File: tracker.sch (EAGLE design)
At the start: 118 parts, among them J1 75869-131LF, J2 5-5530843-0FEMALE, J3 75869-131LF, Q1 DMG2302UK, Q2 CPC1002N, Q3 CPC1002N, Q4 MMBT3904, U1 AOZ6662DI, U2 ATMEGA328PB32-TQFP, U3 MCP1501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

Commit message: Various schematic updates
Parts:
- removed C7, C8: 1uF, radio-tracker:CAPACITOR0603
- removed R6: 10k, radio-tracker:RESISTOR0603
- removed U7: MIC5504, radio-tracker:MIC5504
- added J4: 640456-3, radio-tracker:640456-3
- added R44: 0R, radio-tracker:RESISTOR0603
- LS1: value WT-1205 -> AT-1224-TWT-5V-2-R; device radio-tracker:WT-1205 -> radio-tracker:AT-1224-TWT-5V-2-R
- R3: value 9.1k -> 4.7k
- R4: value 110k -> 68k
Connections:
- removed net +5V: A1.A, C14.P$2, C23.P$2, C6.P$2, C7.P$2, L1.P$2, LS1.P$2, R13.P$2, R4.P$2, R6.P$2, U7.VIN
- removed net N$11: R6.P$1, U7.EN
- new net N$43: C22.P$2
- net +3V3: now also A1.A, C14.P$2, C23.P$2, C6.P$2, L1.P$2, LS1.P$2, R13.P$2, R4.P$2; no longer C22.P$2, C8.P$2, U7.VOUT
- net GND: now also J4.GND; no longer C7.P$1, C8.P$1, U7.GND
- net MISO: now also R44.P$2
- net SCL: now also J4.SCL
- net SDA: now also J4.SDA
- net SLAVE_MISO: now also R44.P$1
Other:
- moved on the sheet: C12, C13, C2, C22, C23, C3, C4, C5, C6, L1, R14, R2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

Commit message: A few schematic updates
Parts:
- added C36, C8: 10uF, radio-tracker:CAPACITOR0805
- added C37: 0.01uF, radio-tracker:CAPACITOR0603
- added C38: 1uF, radio-tracker:CAPACITOR0603
- added C39, C7: 0.1uF, radio-tracker:CAPACITOR0603
- added C40: 22uF, radio-tracker:CAPACITOR0805
- added L2: 2.2uH, radio-tracker:INDUCTOR0805
- added R45, R46, R6: 10k, radio-tracker:RESISTOR0603
- added R47, R48, R49, R50: 0R, radio-tracker:RESISTOR0603
- added R52: 9.1k, radio-tracker:RESISTOR0603
- added R53: 110k, radio-tracker:RESISTOR0603
- added R54: 15k, radio-tracker:RESISTOR0603
- added U7: 47L16, radio-tracker:47L16
- added U8: AOZ6662DI, radio-tracker:AOZ6662DI
- R38: value (none) -> 10k
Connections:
- removed net N$2: S1.3, U1.EN
- new net +5V: C40.P$2, L2.P$2, R48.P$2, R49.P$2, R53.P$2
- new net N$11: R42.P$1, U6.E0
- new net N$44: C8.P$2, U7.VCAP
- new net N$45: R45.P$2, U7.A2
- new net N$46: R46.P$2, U7.A1
- new net N$50: R52.P$2, U8.COMP
- new net N$51: C2.P$2, R49.P$1, R50.P$1, U1.VIN
- new net N$52: C37.P$2, R52.P$1
- new net N$53: C38.P$2, U8.VCC
- new net N$54: C39.P$2, U8.BST
- new net N$55: C39.P$1, L2.P$1, U8.LX
- new net N$56: R53.P$1, R54.P$2, U8.FB
- new net PWR_EN: S1.3, U1.EN, U8.EN
- net +3V3: now also C22.P$2, C7.P$2, R42.P$2, R47.P$2, U7.VCC; no longer A1.A, C23.P$2
- net +7V4V: now also C36.P$2, R50.P$2, U8.VIN; no longer C2.P$2, U1.VIN
- net GND: now also C36.P$1, C37.P$1, C38.P$1, C40.P$1, C7.P$1, C8.P$1, R45.P$1, R46.P$1, R54.P$1, R6.P$1, U7.GND, U8.GND; no longer R42.P$1
- net N$38: now also R6.P$2, U7.HS; no longer R42.P$2, U6.E0
- net N$43: now also A1.A, C23.P$2, R47.P$1, R48.P$1; no longer C22.P$2
- net SCL: now also U7.SCL
- net SDA: now also U7.SDA
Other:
- moved on the sheet: C12, C13, C2, C22, C23, C3, C4, C5, C6, L1, R14, R2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

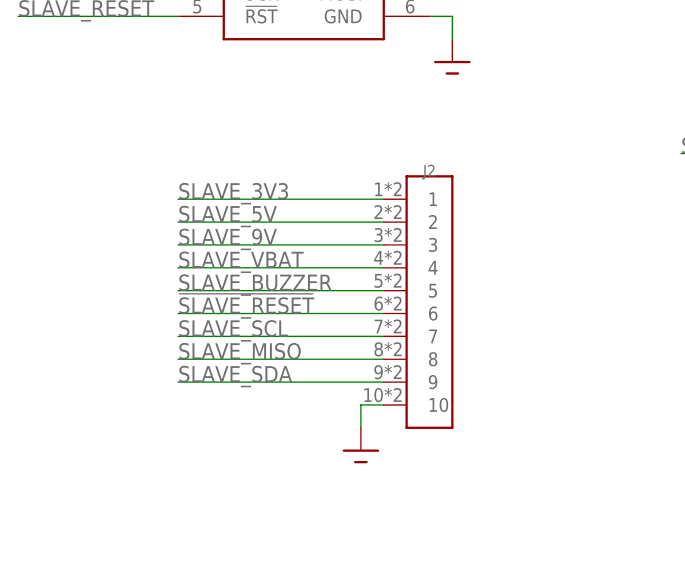
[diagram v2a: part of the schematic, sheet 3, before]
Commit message: Routed beacon
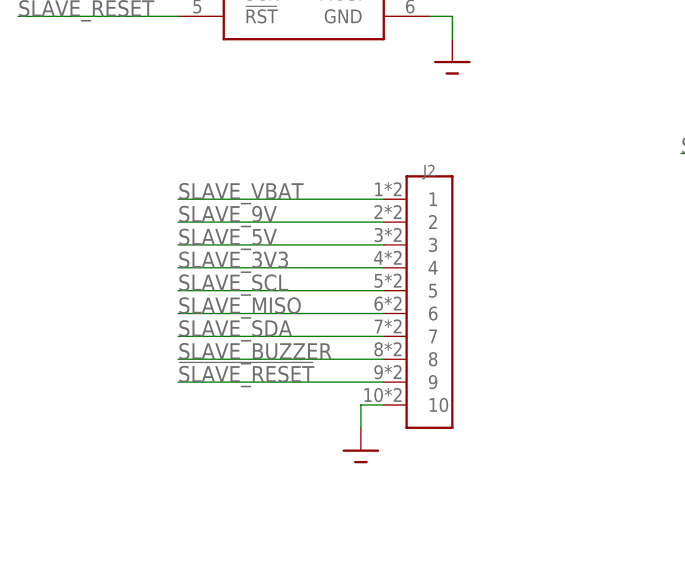
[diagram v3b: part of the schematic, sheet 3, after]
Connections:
- net !SLAVE_RESET: now also J2.9; no longer J2.6
- net SLAVE_3V3: now also J2.4; no longer J2.1
- net SLAVE_5V: now also J2.3; no longer J2.2
- net SLAVE_9V: now also J2.2; no longer J2.3
- net SLAVE_BUZZER: now also J2.8; no longer J2.5
- net SLAVE_MISO: now also J2.6; no longer J2.8
- net SLAVE_SCL: now also J2.5; no longer J2.7
- net SLAVE_SDA: now also J2.7; no longer J2.9
- net SLAVE_VBAT: now also J2.1; no longer J2.4
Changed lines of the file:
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@@
 <net name="SLAVE_SDA" class="0">
+<segment>
+<pinref part="J3" gate="G$1" pin="MOSI"/>
+<wire x1="38.1" y1="38.1" x2="20.32" y2="38.1" width="0.1524" layer="91"/>
+<label x="22.86" y="38.1" size="1.778" layer="95"/>
+</segment>
+<segment>
+<pinref part="J2" gate="G$1" pin="7"/>
+<wire x1="15.24" y1="0" x2="-7.62" y2="0" width="0.1524" layer="91"/>
+<label x="-7.62" y="0" size="1.778" layer="95"/>
+</segment>
+</net>
+<net name="SLAVE_MISO" class="0">
+<segment>
+<pinref part="J3" gate="G$1" pin="MISO"/>
+<wire x1="-7.62" y1="40.64" x2="-25.4" y2="40.64" width="0.1524" layer="91"/>
+<label x="-25.4" y="40.64" size="1.778" layer="95"/>
+</segment>
+<segment>
+<pinref part="R44" gate="G$1" pin="P$1"/>
+<wire x1="15.24" y1="-30.48" x2="-2.54" y2="-30.48" width="0.1524" layer="91"/>
+<label x="-2.54" y="-30.48" size="1.778" layer="95"/>
+</segment>
+<segment>
+<pinref part="J2" gate="G$1" pin="6"/>
+<wire x1="-7.62" y1="2.54" x2="15.24" y2="2.54" width="0.1524" layer="91"/>
+<label x="-7.62" y="2.54" size="1.778" layer="95"/>
+</segment>
+</net>
+<net name="SLAVE_SCL" class="0">
+<segment>
+<pinref part="J3" gate="G$1" pin="SCK"/>
+<wire x1="-25.4" y1="38.1" x2="-7.62" y2="38.1" width="0.1524" layer="91"/>
+<label x="-25.4" y="38.1" size="1.778" layer="95"/>
+</segment>
+<segment>
+<pinref part="J2" gate="G$1" pin="5"/>
+<wire x1="15.24" y1="5.08" x2="-7.62" y2="5.08" width="0.1524" layer="91"/>
+<label x="-7.62" y="5.08" size="1.778" layer="95"/>
+</segment>
+</net>
+<net name="!SLAVE_RESET" class="0">
+<segment>
+<pinref part="J3" gate="G$1" pin="!RST"/>
+<wire x1="-7.62" y1="35.56" x2="-25.4" y2="35.56" width="0.1524" layer="91"/>
+<label x="-25.4" y="35.56" size="1.778" layer="95"/>
+</segment>
 <segment>
 <pinref part="J2" gate="G$1" pin="9"/>
@@
 <label x="-7.62" y="-5.08" size="1.778" layer="95"/>
 </segment>
-<segment>
-<pinref part="J3" gate="G$1" pin="MOSI"/>
-<wire x1="38.1" y1="38.1" x2="20.32" y2="38.1" width="0.1524" layer="91"/>
-<label x="22.86" y="38.1" size="1.778" layer="95"/>
-</segment>
-</net>
-<net name="SLAVE_MISO" class="0">
-<segment>
-<pinref part="J2" gate="G$1" pin="8"/>
-<wire x1="-7.62" y1="-2.54" x2="15.24" y2="-2.54" width="0.1524" layer="91"/>
-<label x="-7.62" y="-2.54" size="1.778" layer="95"/>
-</segment>
-<segment>
-<pinref part="J3" gate="G$1" pin="MISO"/>
-<wire x1="-7.62" y1="40.64" x2="-25.4" y2="40.64" width="0.1524" layer="91"/>
-<label x="-25.4" y="40.64" size="1.778" layer="95"/>
-</segment>
-<segment>
-<pinref part="R44" gate="G$1" pin="P$1"/>
-<wire x1="15.24" y1="-30.48" x2="-2.54" y2="-30.48" width="0.1524" layer="91"/>
-<label x="-2.54" y="-30.48" size="1.778" layer="95"/>
-</segment>
-</net>
-<net name="SLAVE_SCL" class="0">
-<segment>
-<pinref part="J2" gate="G$1" pin="7"/>
-<wire x1="15.24" y1="0" x2="-7.62" y2="0" width="0.1524" layer="91"/>
-<label x="-7.62" y="0" size="1.778" layer="95"/>
-</segment>
-<segment>
-<pinref part="J3" gate="G$1" pin="SCK"/>
-<wire x1="-25.4" y1="38.1" x2="-7.62" y2="38.1" width="0.1524" layer="91"/>
-<label x="-25.4" y="38.1" size="1.778" layer="95"/>
-</segment>
-</net>
-<net name="!SLAVE_RESET" class="0">
-<segment>
-<pinref part="J2" gate="G$1" pin="6"/>
-<wire x1="-7.62" y1="2.54" x2="15.24" y2="2.54" width="0.1524" layer="91"/>
-<label x="-7.62" y="2.54" size="1.778" layer="95"/>
-</segment>
-<segment>
-<pinref part="J3" gate="G$1" pin="!RST"/>
-<wire x1="-7.62" y1="35.56" x2="-25.4" y2="35.56" width="0.1524" layer="91"/>
-<label x="-25.4" y="35.56" size="1.778" layer="95"/>
-</segment>
-</net>
-<net name="SLAVE_BUZZER" class="0">
-<segment>
-<pinref part="J2" gate="G$1" pin="5"/>
-<wire x1="15.24" y1="5.08" x2="-7.62" y2="5.08" width="0.1524" layer="91"/>
-<label x="-7.62" y="5.08" size="1.778" layer="95"/>
-</segment>
 </net>
 <net name="SLAVE_VBAT" class="0">
-<segment>
-<pinref part="J2" gate="G$1" pin="4"/>
-<wire x1="-7.62" y1="7.62" x2="15.24" y2="7.62" width="0.1524" layer="91"/>
-<label x="-7.62" y="7.62" size="1.778" layer="95"/>
-</segment>
 <segment>
 <pinref part="Q2" gate="G$1" pin="DC+"/>
@@
 <label x="165.1" y="10.16" size="1.778" layer="95"/>
 </segment>
+<segment>
+<pinref part="J2" gate="G$1" pin="1"/>
+<wire x1="15.24" y1="15.24" x2="-7.62" y2="15.24" width="0.1524" layer="91"/>
+<label x="-7.62" y="15.24" size="1.778" layer="95"/>
+</segment>
 </net>
 <net name="SLAVE_9V" class="0">
-<segment>
-<pinref part="J2" gate="G$1" pin="3"/>
-<wire x1="15.24" y1="10.16" x2="-7.62" y2="10.16" width="0.1524" layer="91"/>
-<label x="-7.62" y="10.16" size="1.778" layer="95"/>
-</segment>
 <segment>
 <pinref part="Q2" gate="G$1" pin="DC-"/>
@@
 <label x="119.38" y="10.16" size="1.778" layer="95"/>
 </segment>
-</net>
-<net name="SLAVE_5V" class="0">
 <segment>
 <pinref part="J2" gate="G$1" pin="2"/>
@@
 <label x="-7.62" y="12.7" size="1.778" layer="95"/>
 </segment>
+</net>
+<net name="SLAVE_5V" class="0">
 <segment>
 <pinref part="R19" gate="G$1" pin="P$2"/>
@@
 <wire x1="180.34" y1="63.5" x2="165.1" y2="63.5" width="0.1524" layer="91"/>
 <label x="165.1" y="63.5" size="1.778" layer="95"/>
+</segment>
+<segment>
+<pinref part="J2" gate="G$1" pin="3"/>
+<wire x1="15.24" y1="10.16" x2="-7.62" y2="10.16" width="0.1524" layer="91"/>
+<label x="-7.62" y="10.16" size="1.778" layer="95"/>
 </segment>
 </net>
@@
 </segment>
 <segment>
-<pinref part="J2" gate="G$1" pin="1"/>
-<wire x1="15.24" y1="15.24" x2="-7.62" y2="15.24" width="0.1524" layer="91"/>
-<label x="-7.62" y="15.24" size="1.778" layer="95"/>
-</segment>
-<segment>
 <pinref part="R15" gate="G$1" pin="P$2"/>
 <wire x1="134.62" y1="60.96" x2="134.62" y2="63.5" width="0.1524" layer="91"/>
@@
 <label x="119.38" y="63.5" size="1.778" layer="95"/>
 </segment>
+<segment>
+<pinref part="J2" gate="G$1" pin="4"/>
+<wire x1="-7.62" y1="7.62" x2="15.24" y2="7.62" width="0.1524" layer="91"/>
+<label x="-7.62" y="7.62" size="1.778" layer="95"/>
+</segment>
 </net>
 <net name="N$41" class="0">
@@
 </segment>
 </net>
+<net name="SLAVE_BUZZER" class="0">
+<segment>
+<pinref part="J2" gate="G$1" pin="8"/>
+<wire x1="-7.62" y1="-2.54" x2="15.24" y2="-2.54" width="0.1524" layer="91"/>
+<label x="-7.62" y="-2.54" size="1.778" layer="95"/>
+</segment>
+</net>

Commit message: Layed out tracker board
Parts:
- added C41: (no value), radio-tracker:CAPACITOR0603
- added R51: 0R, radio-tracker:RESISTOR0603
- added R55: 10k, radio-tracker:RESISTOR0603
- added RV2: 80mA, radio-tracker:PTC0603
- added RV3: 140mA, radio-tracker:PTC1812
- added RV4, RV5, RV6, RV7, RV8: 50mA, radio-tracker:PTC0603
- R1, R7, R8: device radio-tracker:RESISTOR0805 -> radio-tracker:RESISTOR0603
- XTAL1: device radio-tracker:XRCGB -> radio-tracker:RH100
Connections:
- removed net +3V1: C28.P$2
- removed net +3V2: C29.P$2
- removed net +3V4: C30.P$2
- new net !SLAVE_RAW_RESET: J2.9, J3.!RST, RV4.P$2
- new net N$2: Q3.DC+, RV2.P$1
- new net N$58: BT2.+, R51.P$2, RV3.P$1
- new net N$64: J2.8, RV5.P$2
- new net SLAVE_RAW_MISO: J2.6, J3.MISO, RV7.P$2
- new net SLAVE_RAW_SCL: J2.5, J3.SCK, RV8.P$2
- new net SLAVE_RAW_SDA: J2.7, J3.MOSI, RV6.P$2
- net !RESET: now also R55.P$1
- net !SLAVE_RESET: now also RV4.P$1; no longer J2.9, J3.!RST
- net +3V3: now also C28.P$2, C29.P$2, C30.P$2, R55.P$2, RV2.P$2; no longer Q3.DC+
- net +7V4V: now also RV3.P$2; no longer BT2.+, Q3.DC-
- net BTN0: now also U5.P1_0; no longer U5.P0_0
- net BTN1: now also U5.P0_7; no longer U5.P0_1
- net BTN10: now also U5.P1_4; no longer U5.P1_2
- net BTN11: now also U5.P1_6; no longer U5.P1_3
- net BTN2: now also U5.P0_5; no longer U5.P0_2
- net BTN3: now also U5.P1_1; no longer U5.P0_3
- net BTN4: now also U5.P0_6; no longer U5.P0_4
- net BTN5: now also U5.P0_4; no longer U5.P0_5
- net BTN6: now also U5.P1_2; no longer U5.P0_6
- net BTN7: now also U5.P1_5; no longer U5.P0_7
- net BTN8: now also U5.P1_7; no longer U5.P1_0
- net BTN9: now also U5.P1_3; no longer U5.P1_1
- net DAQ_GPIO0: now also U2.PB7; no longer U2.PB6
- net DAQ_GPIO1: now also U2.PB6; no longer U2.PB7
- net GND: now also XTAL1.GND
- net LED0: now also U5.P0_0; no longer U5.P1_4
- net LED1: now also U5.P0_1; no longer U5.P1_5
- net LED2: now also U5.P0_2; no longer U5.P1_6
- net LED3: now also U5.P0_3; no longer U5.P1_7
- net N$23: now also C41.P$1
- net N$28: now also C41.P$2
- net N$4: now also R51.P$1
- net SLAVE_3V3: now also Q3.DC-
- net SLAVE_BUZZER: now also RV5.P$1; no longer J2.8
- net SLAVE_MISO: now also RV7.P$1; no longer J2.6, J3.MISO
- net SLAVE_SCL: now also RV8.P$1; no longer J2.5, J3.SCK
- net SLAVE_SDA: now also RV6.P$1; no longer J2.7, J3.MOSI
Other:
- moved on the sheet: BT2, C1, Q1, R1, R44
